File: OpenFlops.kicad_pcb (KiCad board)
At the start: 2 copper layers, 111.6 x 59.4 mm, 87 parts, among them P1 FLOPPY_CONN, P10 SD CARD, P11 SD PWR, P12 SD_DISABLE, P2 POWER_INPUT, P3 USB_A_FEMALE, P4 PROG_PORT, P5 JUMPER_JC, P6 ENCODER_PORT, P7 DISPLAY_PORT, P8 USB_HEADER, P9 EXTERNAL_SPEAKER, Q1 BSS138, Q2 BSS138, Q3 BSS138, Q4 BSS138, Q5 BSS138, Q6 BSS138, Q7 MMBT3904, U1 74HCT04, U3 STM32F105RBT6, U4 LM1117-3.3, Y1 8 MHz

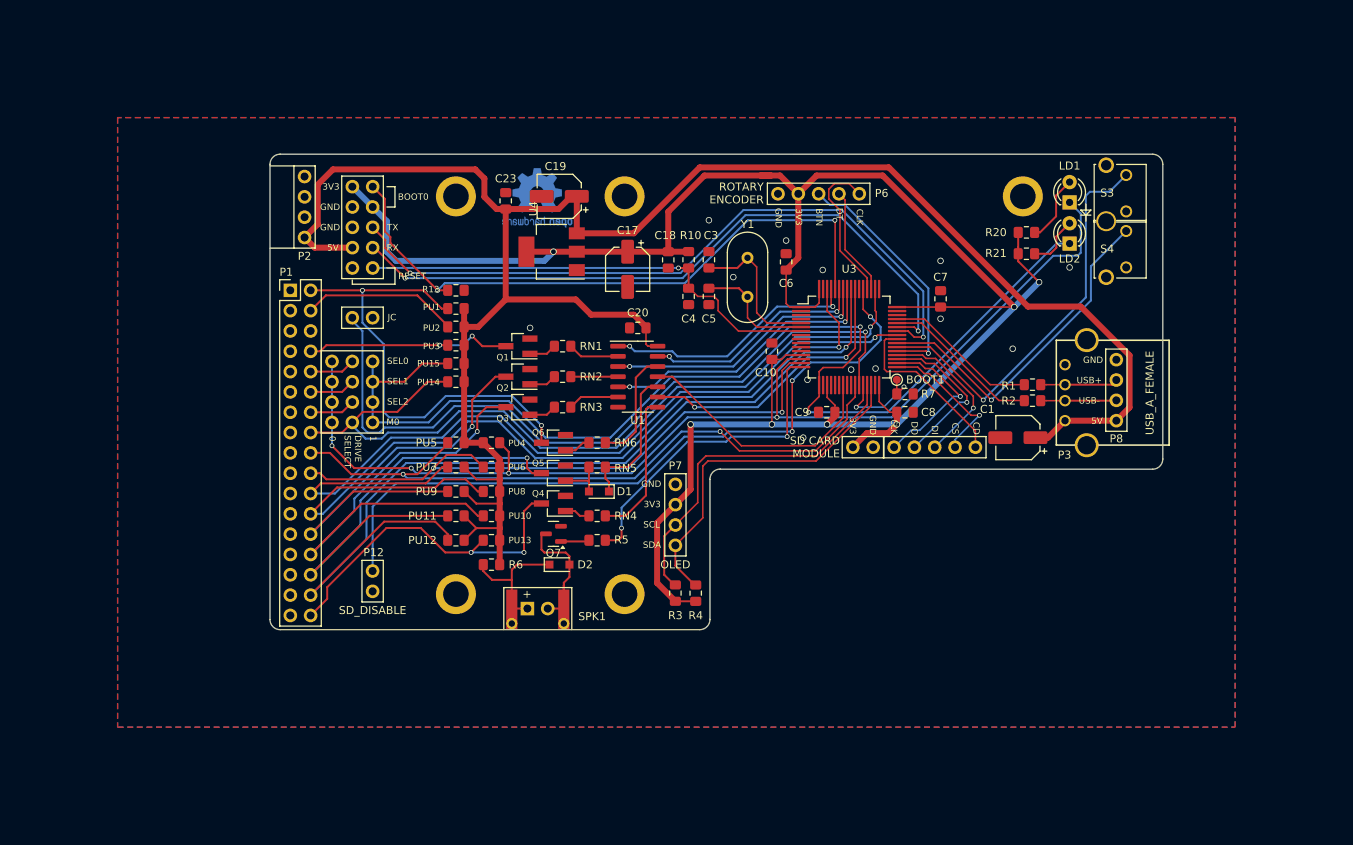
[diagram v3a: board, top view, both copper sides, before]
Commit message: Update footprints
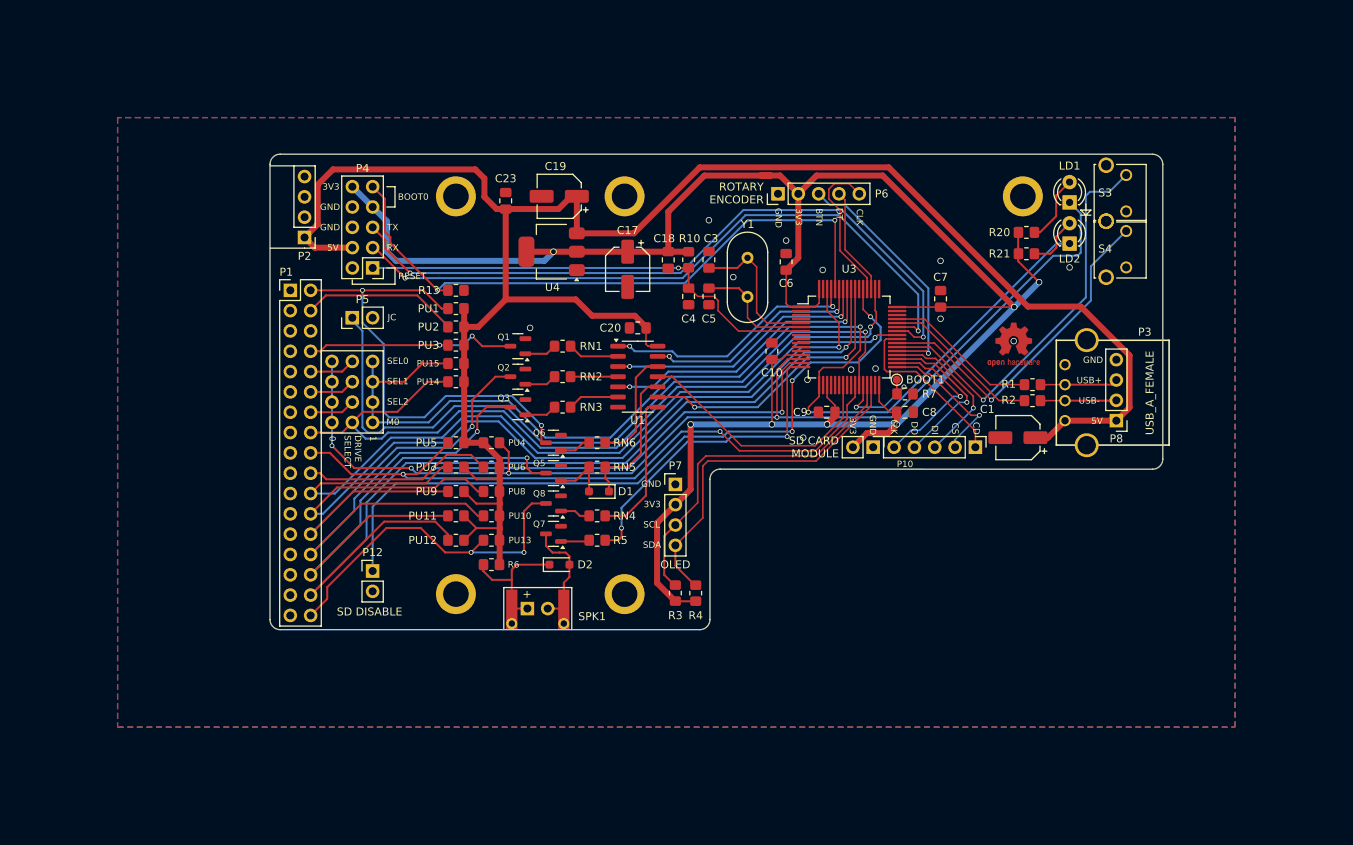
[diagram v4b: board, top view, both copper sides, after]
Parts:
- removed Q4: BSS138, Package_TO_SOT_SMD:SOT-23_Handsoldering
- added Q8: BSS138, Package_TO_SOT_SMD:SOT-23, F.Cu at (130.7, 99.0)
- C10, C18, C20, C23, C3, C4, C5, C6, C7, C8, C9: footprint Capacitor_SMD:C_0805_2012Metric_Pad1.15x1.40mm_HandSolder -> Capacitor_SMD:C_0805_2012Metric_Pad1.18x1.45mm_HandSolder
- P10, P6: footprint OpenFlops:PinHeader_1x05_P2.54mm_Vertical -> Connector_PinHeader_2.54mm:PinHeader_1x05_P2.54mm_Vertical
- P11, P12, P5: footprint OpenFlops:PinHeader_1x02_P2.54mm_Vertical -> Connector_PinHeader_2.54mm:PinHeader_1x02_P2.54mm_Vertical
- P2, P7, P8: footprint OpenFlops:PinHeader_1x04_P2.54mm_Vertical -> Connector_PinHeader_2.54mm:PinHeader_1x04_P2.54mm_Vertical
- P4: footprint OpenFlops:PinHeader_2x05_P2.54mm_Vertical -> Connector_PinHeader_2.54mm:PinHeader_2x05_P2.54mm_Vertical
- PU1, PU10, PU11, PU12, PU13, PU14, PU15, PU2, PU3, PU4, PU5, PU6, PU7, PU8, PU9, R1, R10, R13, R2, R20, R21, R3, R4, R5, R6, R7, RN1, RN2, RN3, RN4, RN5, RN6: footprint Resistor_SMD:R_0805_2012Metric_Pad1.15x1.40mm_HandSolder -> Resistor_SMD:R_0805_2012Metric_Pad1.20x1.40mm_HandSolder
- Q1, Q2, Q3, Q5, Q6: footprint Package_TO_SOT_SMD:SOT-23_Handsoldering -> Package_TO_SOT_SMD:SOT-23
- U4: value LM1117-3.3 -> LM1117MP-3.3
- V0: footprint Symbol:OSHW-Logo2_9.8x8mm_Copper -> Symbol:OSHW-Logo2_7.3x6mm_Copper; moved to F.Cu
- moved V0 62.3 mm to (188.2, 79.2), turned to 0 degrees
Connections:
- net +3V3 renamed +3.3V
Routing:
- net /spk-: track 16.7 -> 15.9 mm
- net Net-(D1-A): track 6.01 -> 6.71 mm
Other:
- board text added: "SD DISABLE"

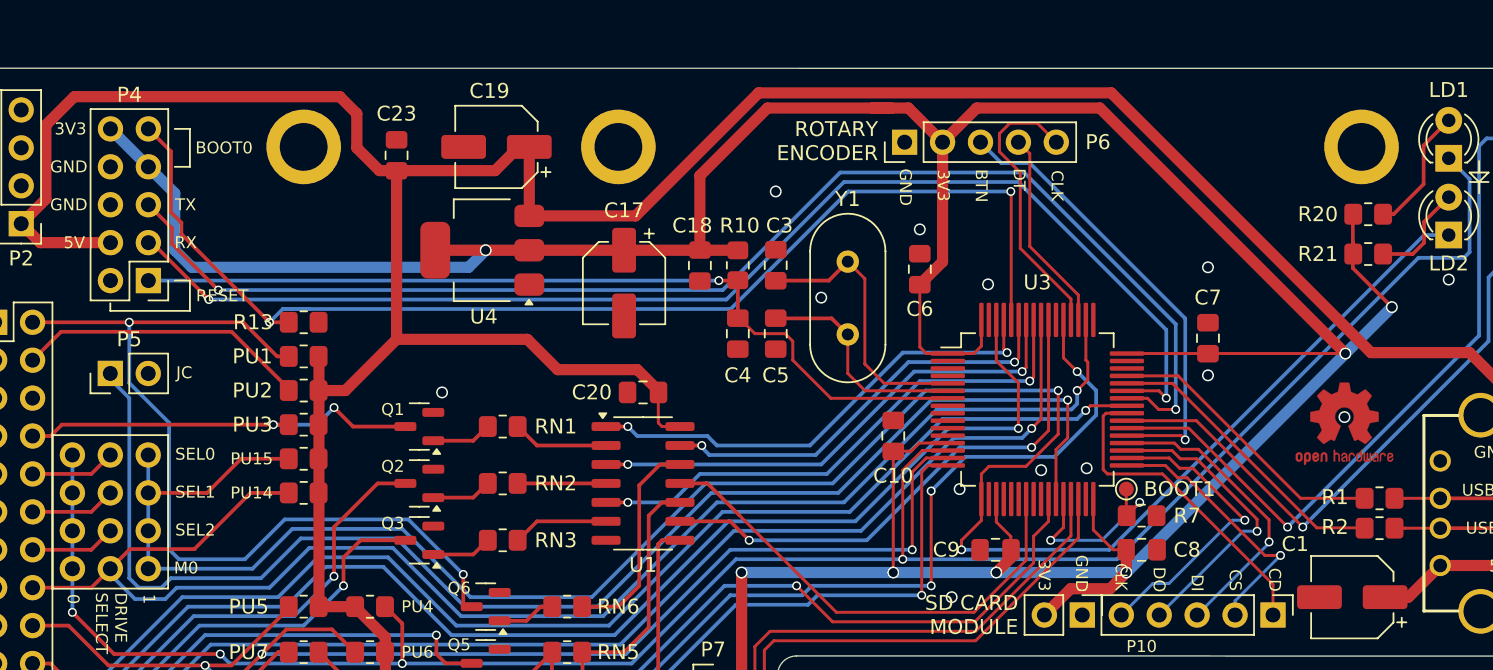
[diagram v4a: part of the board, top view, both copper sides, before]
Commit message: Move license/URL to front
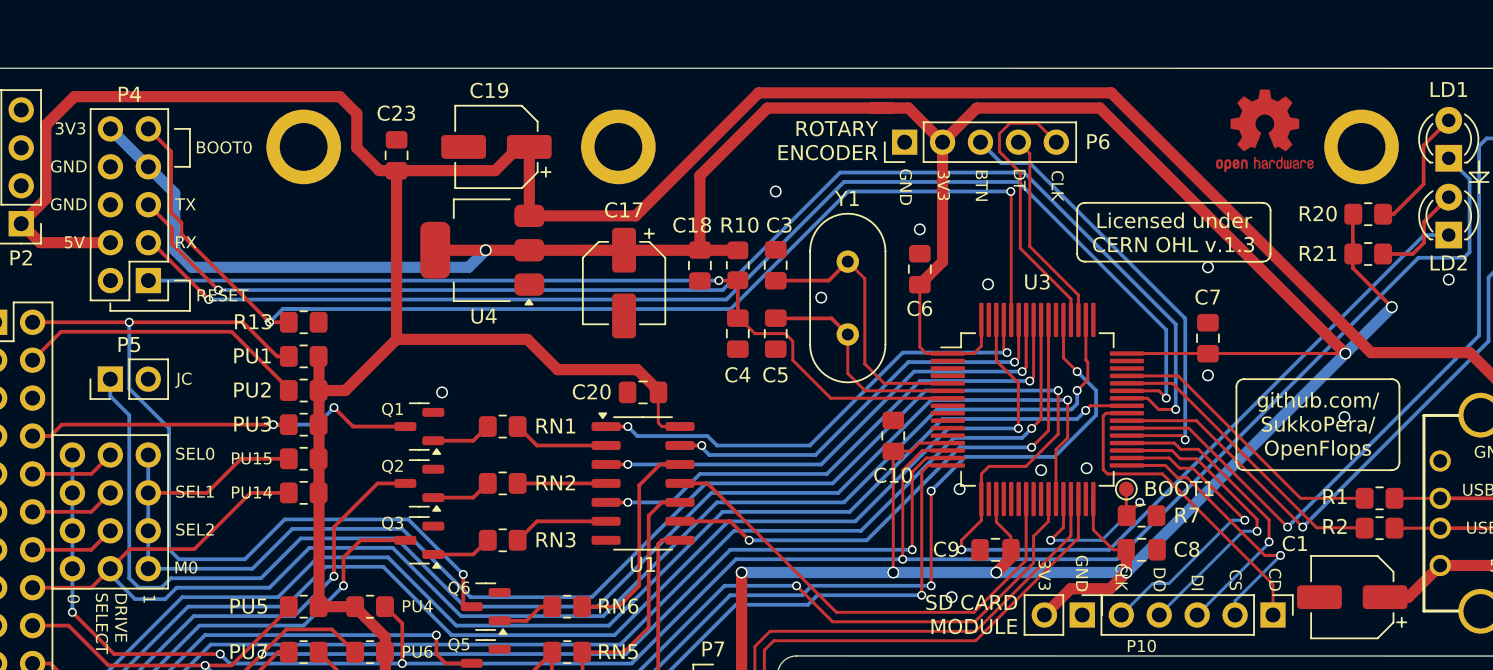
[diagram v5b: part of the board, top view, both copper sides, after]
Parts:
- moved V0 20.3 mm to (182.9, 59.6)
- moved P5 0.38 mm to (105.5, 76.2)
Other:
- board text added: "github.com/ SukkoPera/ OpenFlops"
- board text removed: "github.com/SukkoPera/OpenFlops"
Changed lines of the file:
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@@
 	(footprint "Connector_PinHeader_2.54mm:PinHeader_1x02_P2.54mm_Vertical"
 		(layer "F.Cu")
-		(at 105.537 75.819 90)
+		(at 105.537 76.2 90)
 		(descr "Through hole straight pin header, 1x02, 2.54mm pitch, single row")
 		(tags "Through hole pin header THT 1x02 2.54mm single row")
@@
 	(footprint "Symbol:OSHW-Logo2_7.3x6mm_Copper"
 		(layer "F.Cu")
-		(at 188.214 79.1845)
+		(at 182.88 59.563)
 		(descr "Open Source Hardware Symbol")
 		(tags "Logo Symbol OSHW")
@@
 		)
 	)
+	(gr_arc
+		(start 180.975 76.708)
+		(mid 181.12379 76.34879)
+		(end 181.483 76.2)
+		(stroke
+			(width 0.12)
+			(type default)
+		)
+		(layer "F.SilkS")
+	)
+	(gr_arc
+		(start 170.307 64.897)
+		(mid 170.45579 64.53779)
+		(end 170.815 64.389)
+		(stroke
+			(width 0.12)
+			(type default)
+		)
+		(layer "F.SilkS")
+	)
+	(gr_line
+		(start 182.753 68.326)
+		(end 170.815 68.326)
+		(stroke
+			(width 0.12)
+			(type default)
+		)
+		(layer "F.SilkS")
+	)
 	(gr_line
 		(start 98.238 56.836)
@@
 	)
 	(gr_line
+		(start 180.975 81.788)
+		(end 180.975 76.708)
+		(stroke
+			(width 0.12)
+			(type default)
+		)
+		(layer "F.SilkS")
+	)
+	(gr_line
+		(start 181.483 76.2)
+		(end 191.389 76.2)
+		(stroke
+			(width 0.12)
+			(type default)
+		)
+		(layer "F.SilkS")
+	)
+	(gr_line
 		(start 109.855 59.436)
 		(end 110.871 59.436)
@@
 	)
 	(gr_line
+		(start 170.307 67.818)
+		(end 170.307 64.897)
+		(stroke
+			(width 0.12)
+			(type default)
+		)
+		(layer "F.SilkS")
+	)
+	(gr_line
 		(start 197.231 62.992)
 		(end 196.596 62.357)
@@
 	)
 	(gr_line
+		(start 191.389 82.296)
+		(end 181.483 82.296)
+		(stroke
+			(width 0.12)
+			(type default)
+		)
+		(layer "F.SilkS")
+	)
+	(gr_arc
+		(start 191.897 81.788)
+		(mid 191.74821 82.14721)
+		(end 191.389 82.296)
+		(stroke
+			(width 0.12)
+			(type default)
+		)
+		(layer "F.SilkS")
+	)
+	(gr_line
 		(start 105.537 71.628)
 		(end 110.871 71.628)
@@
 		(layer "F.SilkS")
 	)
+	(gr_arc
+		(start 181.483 82.296)
+		(mid 181.12379 82.14721)
+		(end 180.975 81.788)
+		(stroke
+			(width 0.12)
+			(type default)
+		)
+		(layer "F.SilkS")
+	)
+	(gr_arc
+		(start 182.753 64.389)
+		(mid 183.11221 64.53779)
+		(end 183.261 64.897)
+		(stroke
+			(width 0.12)
+			(type default)
+		)
+		(layer "F.SilkS")
+	)
 	(gr_line
 		(start 99.568 67.116)
@@
 	)
 	(gr_line
+		(start 183.261 64.897)
+		(end 183.261 67.818)
+		(stroke
+			(width 0.12)
+			(type default)
+		)
+		(layer "F.SilkS")
+	)
+	(gr_line
+		(start 191.897 76.708)
+		(end 191.897 81.788)
+		(stroke
+			(width 0.12)
+			(type default)
+		)
+		(layer "F.SilkS")
+	)
+	(gr_line
 		(start 197.231 62.357)
 		(end 197.231 61.595)
@@
 		(layer "F.SilkS")
 	)
+	(gr_arc
+		(start 183.261 67.818)
+		(mid 183.11221 68.17721)
+		(end 182.753 68.326)
+		(stroke
+			(width 0.12)
+			(type default)
+		)
+		(layer "F.SilkS")
+	)
+	(gr_arc
+		(start 170.815 68.326)
+		(mid 170.45579 68.17721)
+		(end 170.307 67.818)
+		(stroke
+			(width 0.12)
+			(type default)
+		)
+		(layer "F.SilkS")
+	)
+	(gr_line
+		(start 170.815 64.389)
+		(end 182.753 64.389)
+		(stroke
+			(width 0.12)
+			(type default)
+		)
+		(layer "F.SilkS")
+	)
 	(gr_line
 		(start 109.407 79.95)
@@
 		(layer "F.SilkS")
 	)
+	(gr_arc
+		(start 191.389 76.2)
+		(mid 191.74821 76.34879)
+		(end 191.897 76.708)
+		(stroke
+			(width 0.12)
+			(type default)
+		)
+		(layer "F.SilkS")
+	)
 	(gr_line
 		(start 110.871 61.976)
@@
 		(layer "Edge.Cuts")
 	)
-	(gr_text "Licensed under CERN OHL v.1.3"
-		(at 122.682 103.251 0)
-		(layer "B.SilkS")
-		(effects
-			(font
-				(size 1 1)
-				(thickness 0.15)
-			)
-			(justify mirror)
-		)
-	)
-	(gr_text "github.com/SukkoPera/OpenFlops"
-		(at 122.682 100.457 0)
-		(layer "B.SilkS")
-		(effects
-			(font
-				(size 1 1)
-				(thickness 0.15)
-			)
-			(justify mirror)
-		)
-	)
 	(gr_text "V2"
 		(at 147.828 113.411 0)
@@
 	)
 	(gr_text "JC"
-		(at 110.49 75.765 0)
+		(at 110.49 76.2 0)
 		(layer "F.SilkS")
 		(effects
@@
 		)
 	)
+	(gr_text "Licensed under\nCERN OHL v.1.3"
+		(at 176.784 66.421 0)
+		(layer "F.SilkS")
+		(effects
+			(font
+				(size 1 1)
+				(thickness 0.15)
+			)
+		)
+	)
 	(gr_text "TX"
 		(at 110.585428 64.516 0)
@@
 		)
 	)
+	(gr_text "github.com/\nSukkoPera/\nOpenFlops"
+		(at 186.436 79.248 0)
+		(layer "F.SilkS")
+		(effects
+			(font
+				(size 1 1)
+				(thickness 0.15)
+			)
+		)
+	)
 	(gr_text "CD"
 		(at 183.54 89.642953 270)
@@
 	)
 	(segment
-		(start 114.554 88.265)
-		(end 110.1344 88.265)
+		(start 129.183 89.281)
+		(end 125.5 85.598)
 		(width 0.25)
 		(layer "B.Cu")
@@
 	)
 	(segment
-		(start 106.807 76.454)
+		(start 106.807 76.835)
 		(end 106.807 72.39)
 		(width 0.25)
@@
 	)
 	(segment
-		(start 129.183 89.281)
-		(end 125.5 85.598)
+		(start 109.474 87.6046)
+		(end 109.474 79.502)
 		(width 0.25)
 		(layer "B.Cu")
@@
 	)
 	(segment
-		(start 117.221 85.598)
-		(end 114.554 88.265)
+		(start 114.554 88.265)
+		(end 110.1344 88.265)
 		(width 0.25)
 		(layer "B.Cu")
@@
 	)
 	(segment
-		(start 110.1344 88.265)
-		(end 109.474 87.6046)
+		(start 109.474 79.502)
+		(end 106.807 76.835)
 		(width 0.25)
 		(layer "B.Cu")
@@
 	)
 	(segment
-		(start 109.474 87.6046)
-		(end 109.474 79.121)
+		(start 117.221 85.598)
+		(end 114.554 88.265)
 		(width 0.25)
 		(layer "B.Cu")
@@
 	)
 	(segment
-		(start 109.474 79.121)
-		(end 106.807 76.454)
+		(start 110.1344 88.265)
+		(end 109.474 87.6046)
 		(width 0.25)
 		(layer "B.Cu")
@@
 	)
 	(segment
-		(start 154.305 83.82)
-		(end 160.528 77.597)
+		(start 105.537 76.2)
+		(end 105.537 77.343)
 		(width 0.25)
 		(layer "B.Cu")
@@
 	)
 	(segment
-		(start 106.807 77.47)
-		(end 106.807 89.535)
+		(start 106.807 89.535)
+		(end 107.442 90.17)
 		(width 0.25)
 		(layer "B.Cu")
@@
 	)
 	(segment
-		(start 129.286 91.44)
-		(end 138.176 91.44)
+		(start 107.442 90.17)
+		(end 108.966 90.17)
 		(width 0.25)
 		(layer "B.Cu")
@@
 	)
 	(segment
-		(start 109.601 89.535)
-		(end 115.6335 89.535)
+		(start 115.6335 89.535)
+		(end 118.3005 86.868)
 		(width 0.25)
 		(layer "B.Cu")
@@
 	)
 	(segment
-		(start 124.714 86.868)
-		(end 129.286 91.44)
+		(start 145.796 83.82)
+		(end 154.305 83.82)
 		(width 0.25)
 		(layer "B.Cu")
@@
 	)
 	(segment
-		(start 145.796 83.82)
-		(end 154.305 83.82)
+		(start 160.528 77.597)
+		(end 169.672 77.597)
 		(width 0.25)
 		(layer "B.Cu")
@@
 	)
 	(segment
-		(start 108.966 90.17)
-		(end 109.601 89.535)
+		(start 154.305 83.82)
+		(end 160.528 77.597)
 		(width 0.25)
 		(layer "B.Cu")
@@
 	)
 	(segment
-		(start 107.442 90.17)
-		(end 108.966 90.17)
+		(start 106.807 78.613)
+		(end 106.807 89.535)
 		(width 0.25)
 		(layer "B.Cu")
@@
 	)
 	(segment
-		(start 115.6335 89.535)
-		(end 118.3005 86.868)
+		(start 124.714 86.868)
+		(end 129.286 91.44)
 		(width 0.25)
 		(layer "B.Cu")
@@
 	)
 	(segment
-		(start 118.3005 86.868)
-		(end 124.714 86.868)
+		(start 108.966 90.17)
+		(end 109.601 89.535)
 		(width 0.25)
 		(layer "B.Cu")
@@
 	)
 	(segment
-		(start 105.537 76.2)
-		(end 106.807 77.47)
+		(start 105.537 77.343)
+		(end 106.807 78.613)
 		(width 0.25)
 		(layer "B.Cu")
@@
 	)
 	(segment
-		(start 160.528 77.597)
-		(end 169.672 77.597)
+		(start 138.176 91.44)
+		(end 145.796 83.82)
 		(width 0.25)
 		(layer "B.Cu")
@@
 	)
 	(segment
-		(start 106.807 89.535)
-		(end 107.442 90.17)
+		(start 129.286 91.44)
+		(end 138.176 91.44)
 		(width 0.25)
 		(layer "B.Cu")
@@
 	)
 	(segment
-		(start 138.176 91.44)
-		(end 145.796 83.82)
+		(start 109.601 89.535)
+		(end 115.6335 89.535)
+		(width 0.25)
+		(layer "B.Cu")
+		(net 30)
+	)
+	(segment
+		(start 118.3005 86.868)
+		(end 124.714 86.868)
 		(width 0.25)
 		(layer "B.Cu")

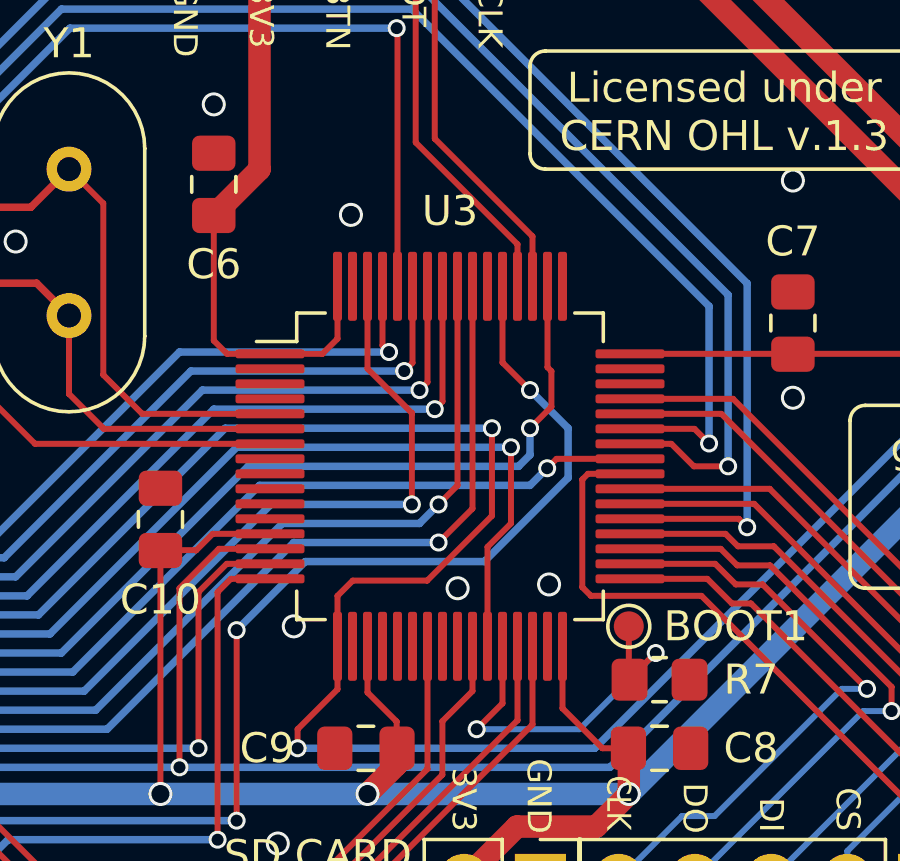
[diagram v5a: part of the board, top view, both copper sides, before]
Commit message: Update MCU footprint MCU and MOSFET are no longer "handsolder", not sure if it's OK...
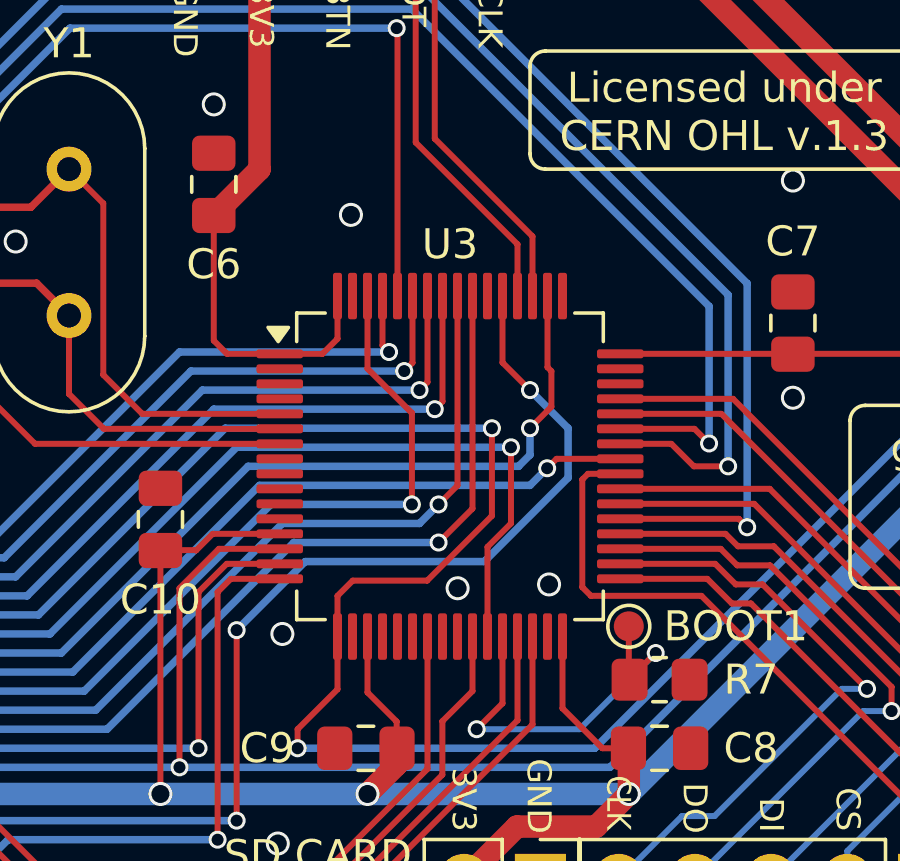
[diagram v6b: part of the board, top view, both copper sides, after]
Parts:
- U3: footprint OpenFlops:LQFP-64_Handsoldering -> Package_QFP:LQFP-64_10x10mm_P0.5mm
